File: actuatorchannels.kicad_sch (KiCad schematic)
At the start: 102 parts, among them J10 ACT CH9, J11 ACT CH10, J12 ACT CH11, J13 ACT CH12, J14 ACT CH13, J15 ACT CH14, J16 ACT CH15, J17 ACT CH16, J2 ACT CH1, J3 ACT CH2, J4 ACT CH3, J5 ACT CH4, J6 ACT CH5, J7 ACT CH6, J8 ACT CH7, J9 ACT CH8, U10 TLP241A, U11 TLP241A, U12 TLP241A, U13 TLP241A, U14 TLP241A, U15 TLP241A, U16 TLP241A, U17 TLP241A, U18 TLP241A, U19 PCA9534, U20 PCA9534, U3 TLP241A, U4 TLP241A, U5 TLP241A, U6 TLP241A, U7 TLP241A, U8 TLP241A, U9 TLP241A

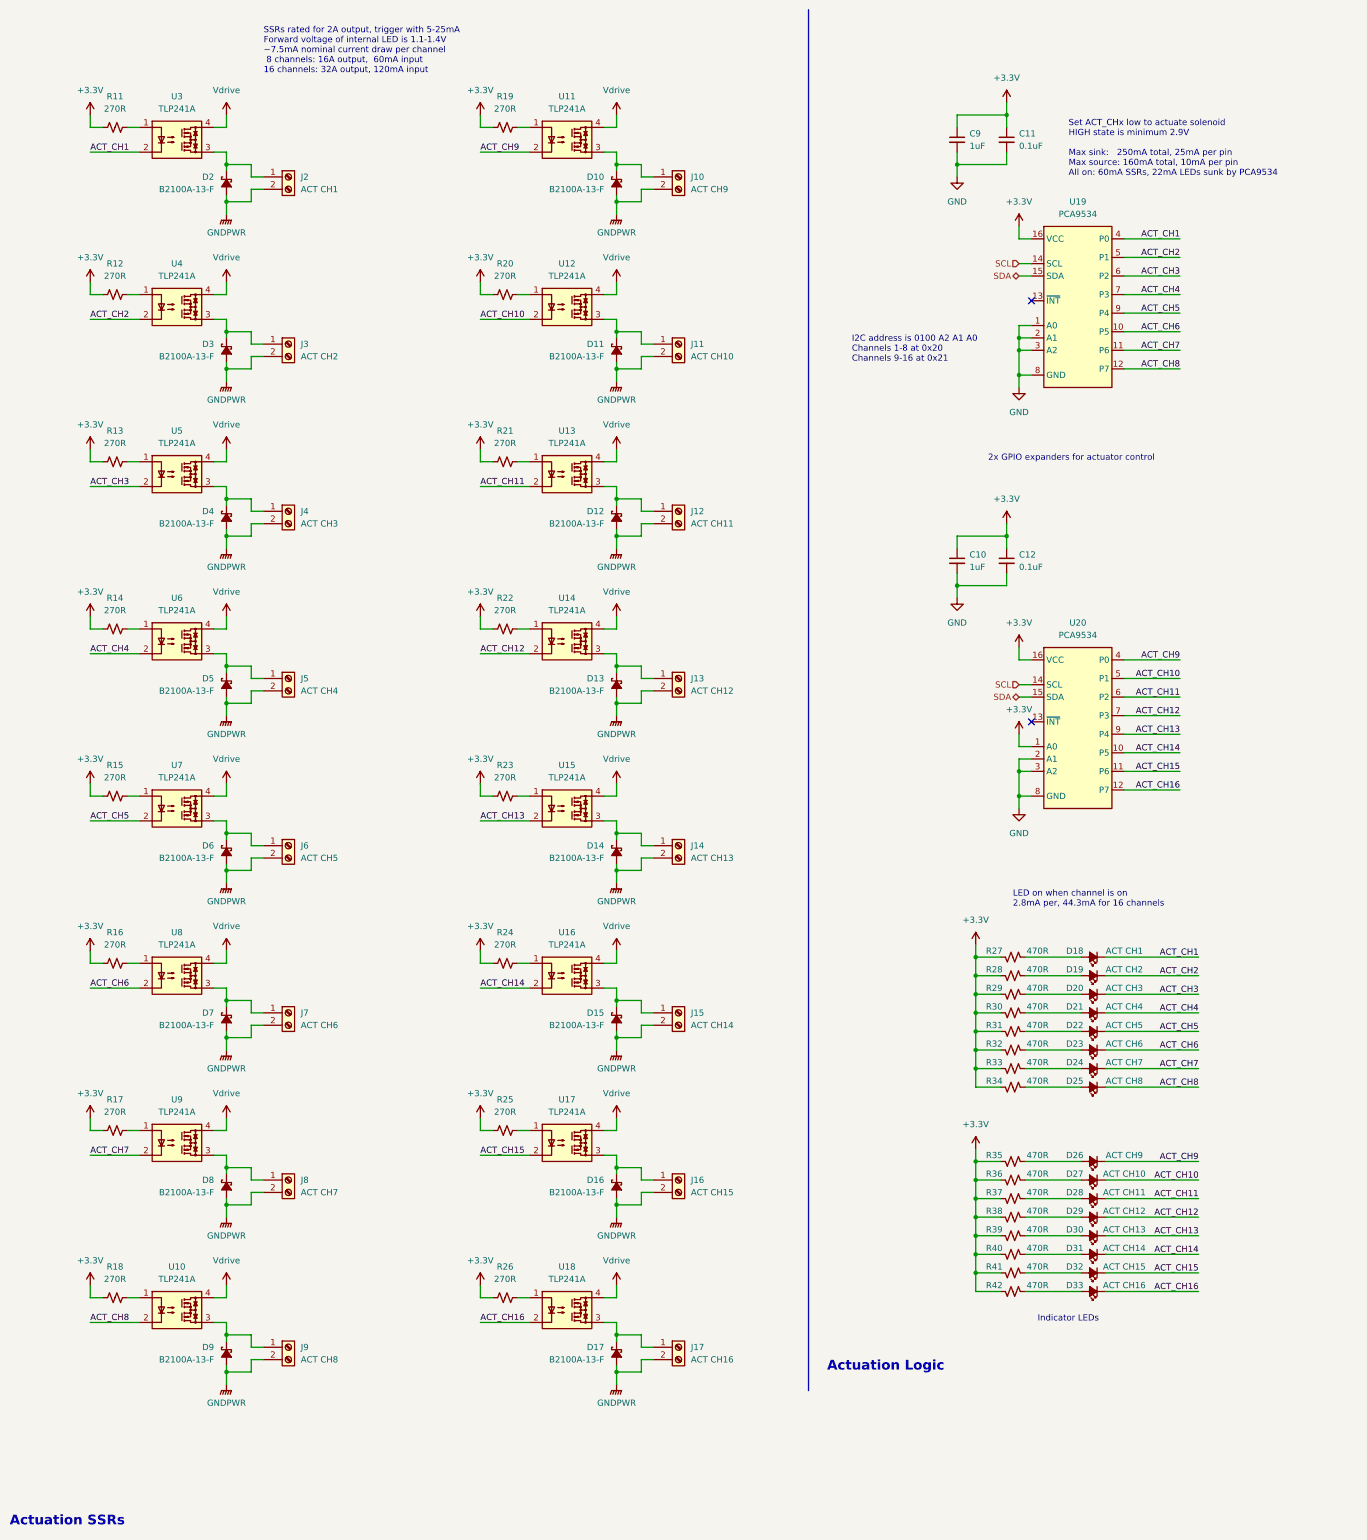
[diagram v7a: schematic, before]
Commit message: Safing jumper, status LEDs, better naming of power states
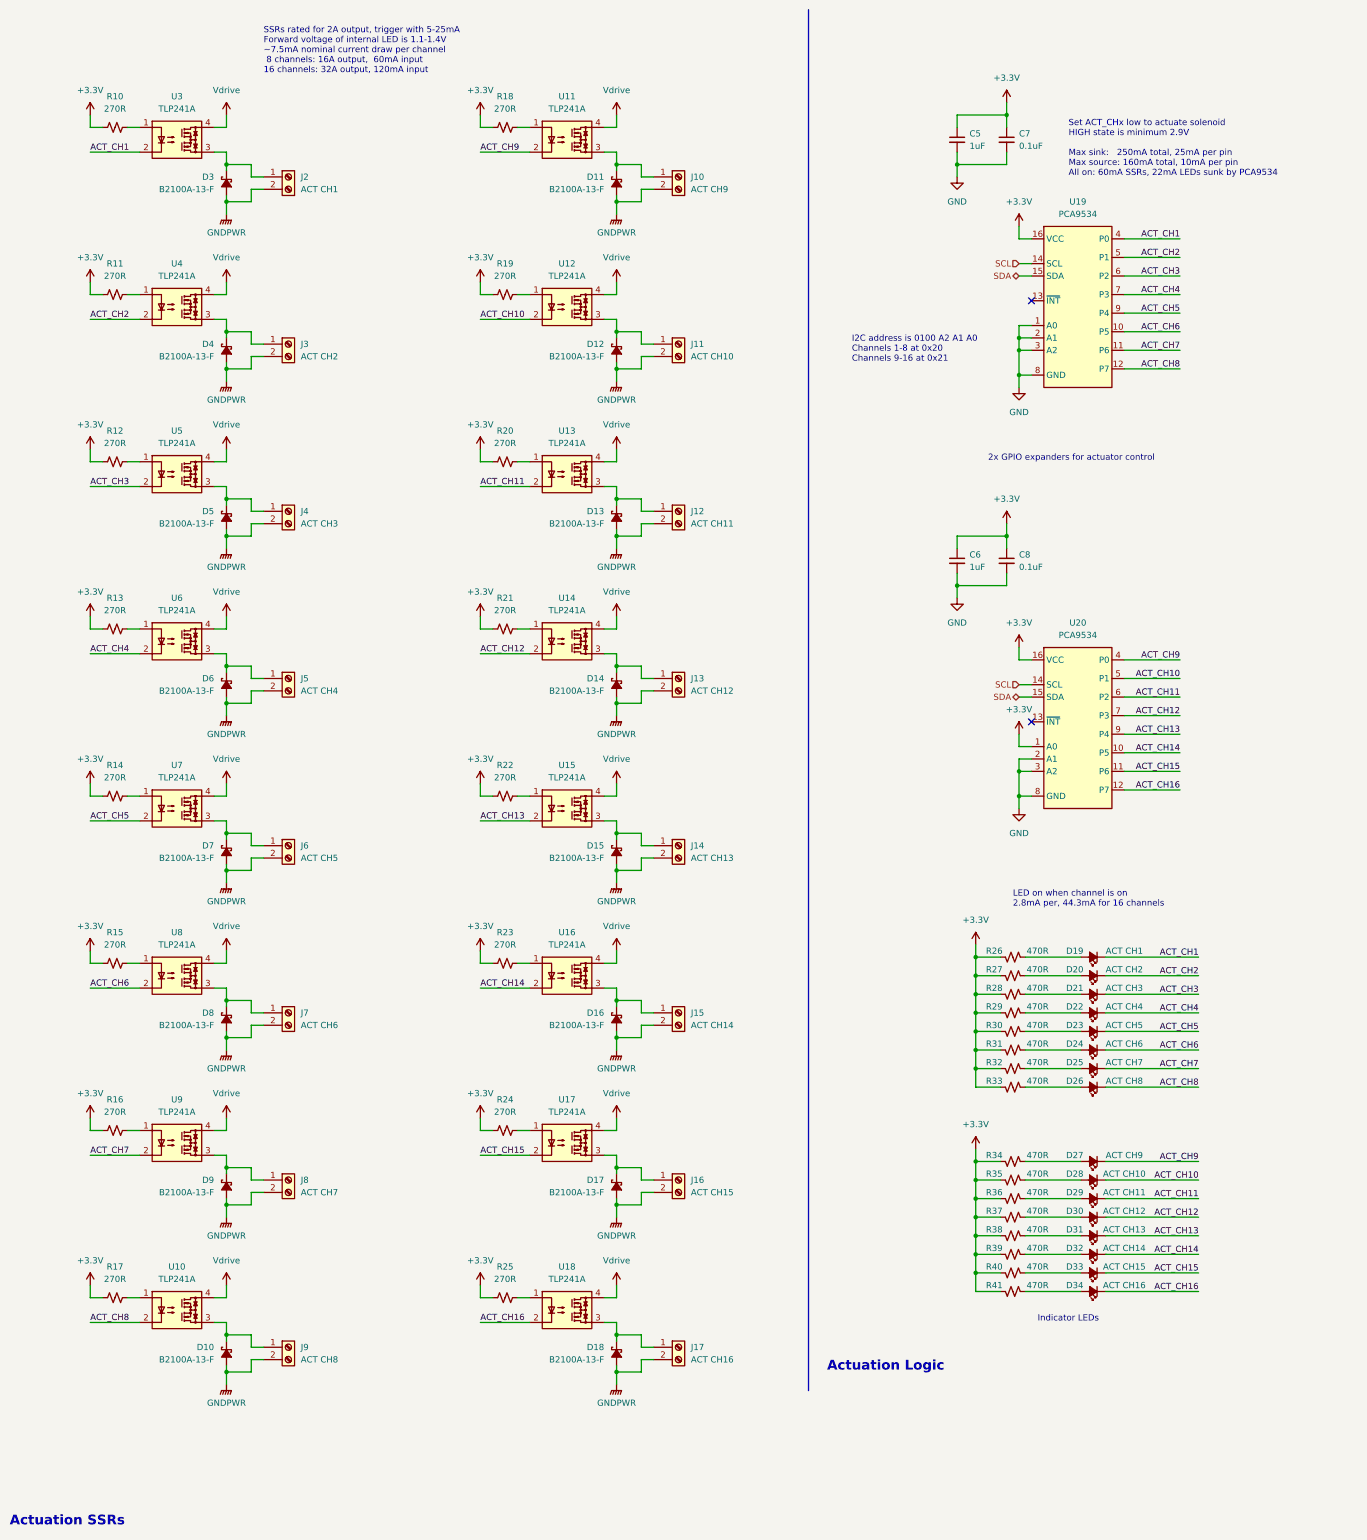
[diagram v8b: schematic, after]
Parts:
- D19: renamed from D18; MPN LTST-C191KRKT -> LTST-C191KFKT
- D20: renamed from D19; MPN LTST-C191KRKT -> LTST-C191KFKT
- D21: renamed from D20; MPN LTST-C191KRKT -> LTST-C191KFKT
- D22: renamed from D21; MPN LTST-C191KRKT -> LTST-C191KFKT
- D23: renamed from D22; MPN LTST-C191KRKT -> LTST-C191KFKT
- D24: renamed from D23; MPN LTST-C191KRKT -> LTST-C191KFKT
- D25: renamed from D24; MPN LTST-C191KRKT -> LTST-C191KFKT
- D26: renamed from D25; MPN LTST-C191KRKT -> LTST-C191KFKT
- D27: renamed from D26; MPN LTST-C191KRKT -> LTST-C191KFKT
- D28: renamed from D27; MPN LTST-C191KRKT -> LTST-C191KFKT
- D29: renamed from D28; MPN LTST-C191KRKT -> LTST-C191KFKT
- D30: renamed from D29; MPN LTST-C191KRKT -> LTST-C191KFKT
- D31: renamed from D30; MPN LTST-C191KRKT -> LTST-C191KFKT
- D32: renamed from D31; MPN LTST-C191KRKT -> LTST-C191KFKT
- D33: renamed from D32; MPN LTST-C191KRKT -> LTST-C191KFKT
- D34: renamed from D33; MPN LTST-C191KRKT -> LTST-C191KFKT
- renumbered C9 to C5, C10 to C6, C11 to C7, C12 to C8, D9 to D10, D10 to D11, D11 to D12, D12 to D13, D13 to D14, D14 to D15, D15 to D16, D16 to D17, D17 to D18, D2 to D3, D3 to D4, D4 to D5, D5 to D6, D6 to D7, D7 to D8, D8 to D9, R11 to R10, R12 to R11, R13 to R12, R14 to R13, R15 to R14, R16 to R15, R17 to R16, R18 to R17, R19 to R18, R20 to R19, R21 to R20, R22 to R21, R23 to R22, R24 to R23, R25 to R24, R26 to R25, R27 to R26, R28 to R27, R29 to R28, R30 to R29, R31 to R30, R32 to R31, R33 to R32, R34 to R33, R35 to R34, R36 to R35, R37 to R36, R38 to R37, R39 to R38, R40 to R39, R41 to R40, R42 to R41
